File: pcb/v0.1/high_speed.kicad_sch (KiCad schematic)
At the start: 20 parts, among them J4 TYPE_C_Receptacle, J5 TYPE_C_Receptacle, J6 22s_disp_connector, J7 ComputeModule5-CM5_connector, U2 Nexperia PUSB3FR4Z, U3 Nexperia PUSB3FR4Z, U8 AP22653W6-7

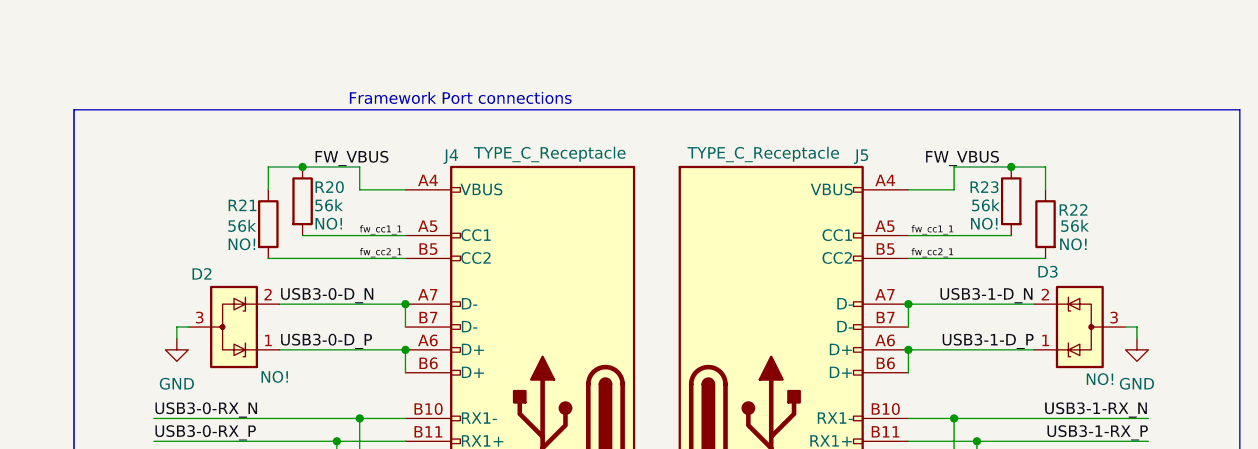
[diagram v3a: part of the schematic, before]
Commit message: Finish ESD protection.
There are now TVS diodes/arrays on both the signal lines and power lines
in every user accessible connector. Such as USBc ports and GPIO.

I have not included them for internal headers, jumpers or connectors
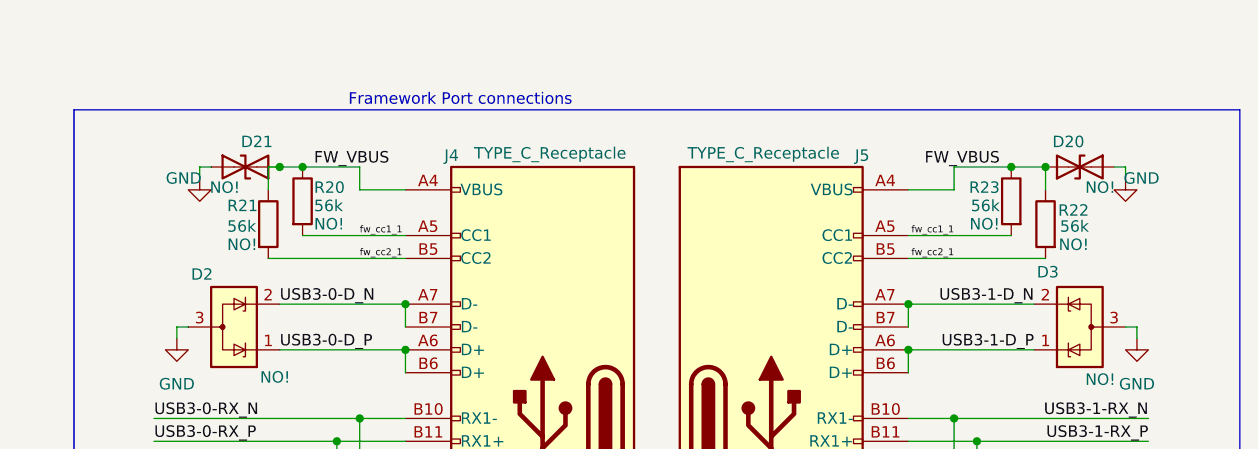
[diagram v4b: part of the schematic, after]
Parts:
- added D20, D21: TVS_DIODE_7.1VC, Diode_SMD:D_SOD-882, symbol TH-1-CC:TVS_DIODE_7.1VC
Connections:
- net FW_VBUS: now also D20.1 (A1), D21.1 (A1)
- net GND: now also D20.2 (A2), D21.2 (A2)
